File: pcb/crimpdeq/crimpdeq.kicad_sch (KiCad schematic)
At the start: 55 parts, among them J10 A-_Cable_Pad, J11 E+_Cable_Pad, J12 E-_Cable_Pad, J2 USB4105-GF-A, J5 B-_Cable_Pad, J6 SW+_Cable_Pad, J7 B+_Cable_Pad, J8 SW-_Cable_Pad, J9 A+_Cable_Pad, Q2 DMG3415U, U1 ESP32-C3-MINI-1, U2 MCP73831T-2ACI/OT, U3 ADS1220, U5 MAX17048G+T10, U6 SY8088

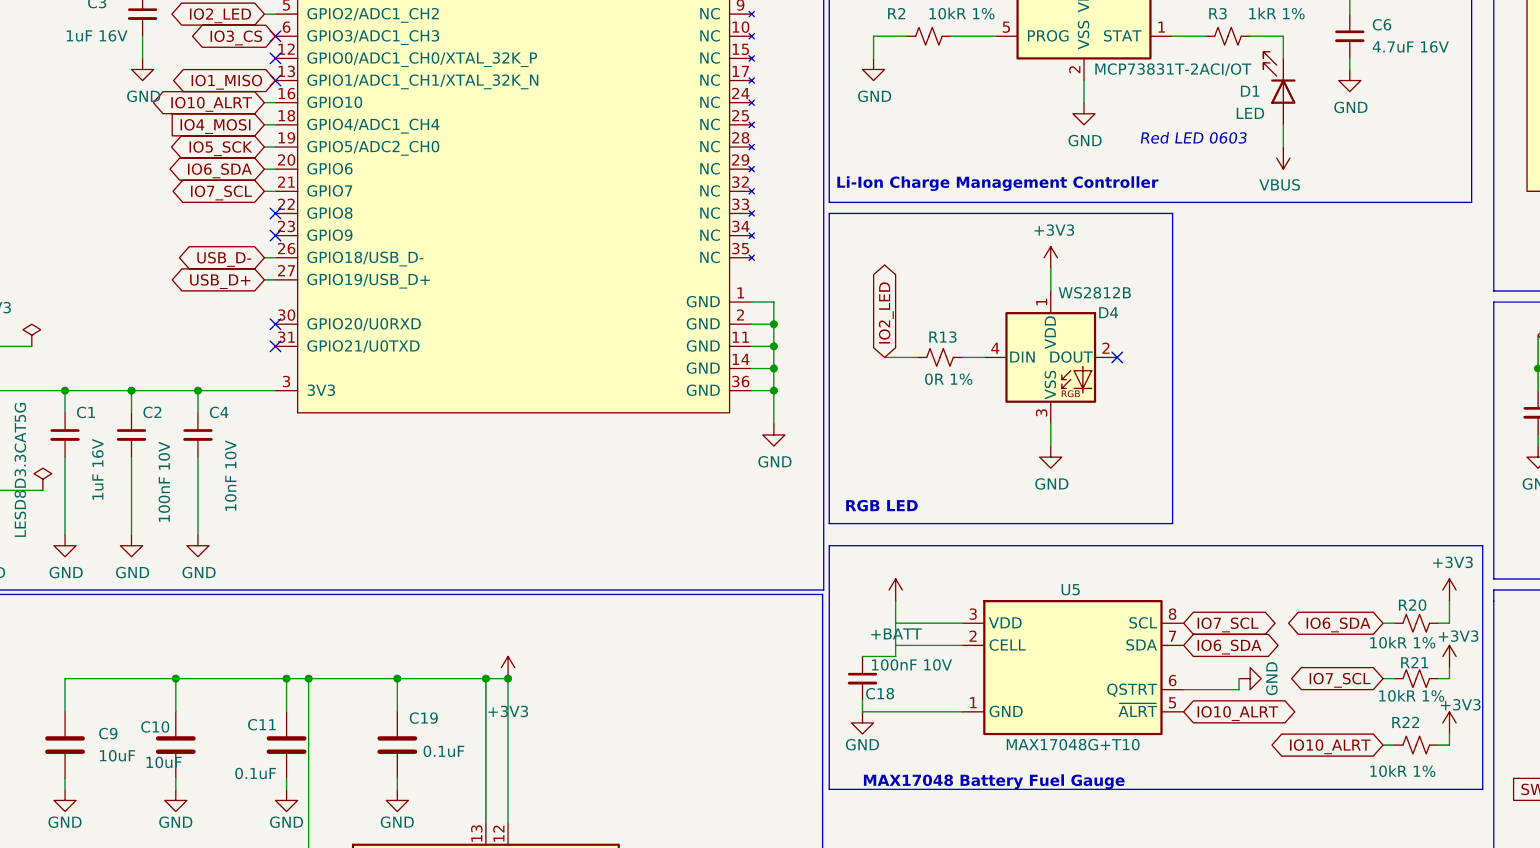
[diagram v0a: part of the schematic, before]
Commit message: fix: align MAX17048 I2C names with TDFN pads
Keep existing copper and GPIO numbers; rename the reversed SDA/SCL
labels and restore missing schematic paths so the board matches the
datasheet pin map.

Co-authored-by: Cursor <cursoragent@cursor.com>
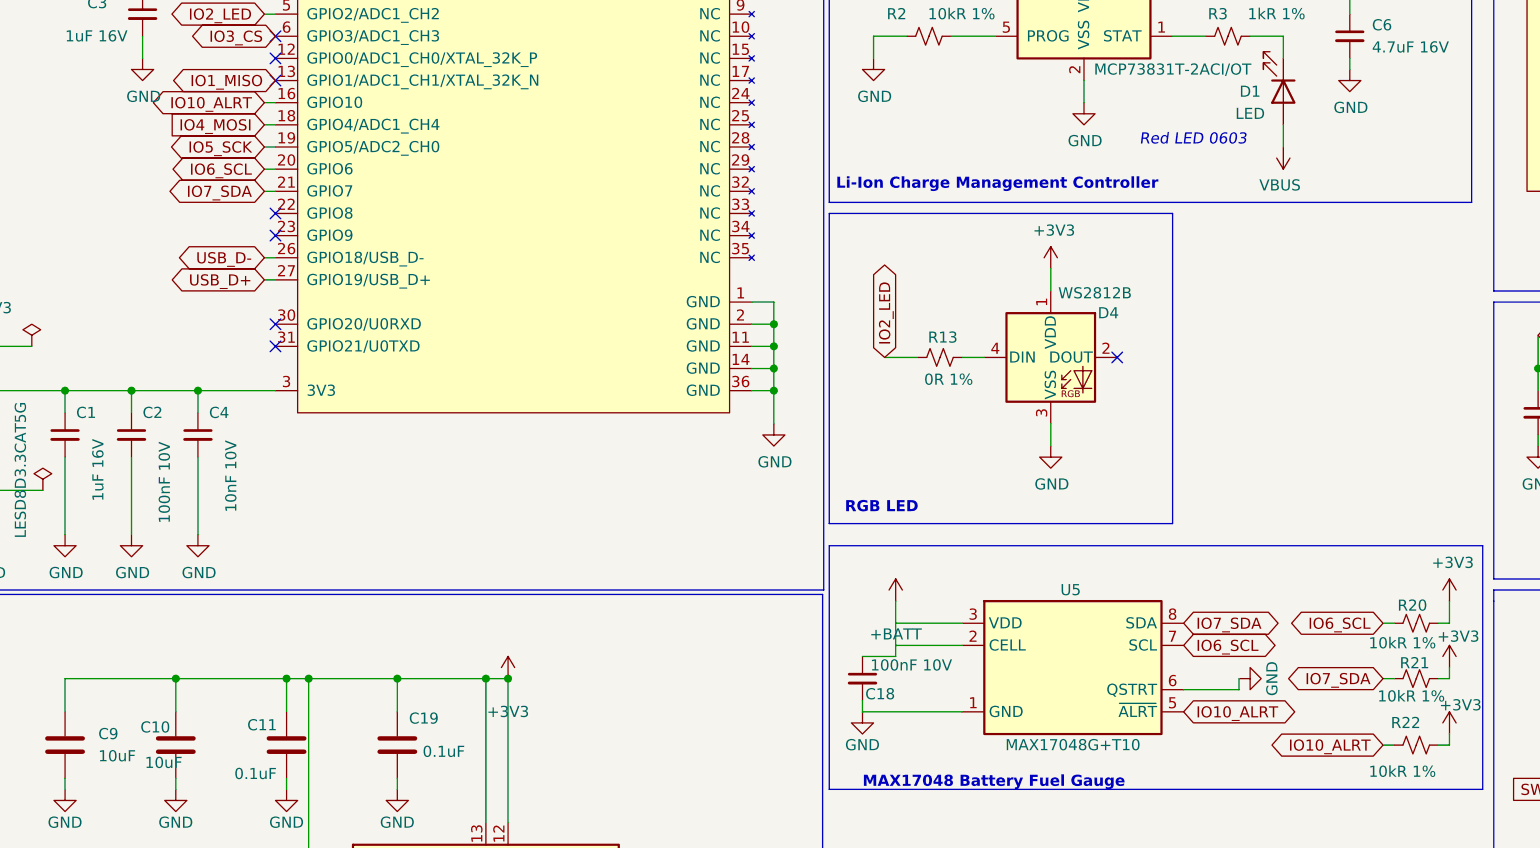
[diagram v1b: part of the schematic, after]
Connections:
- net IO6_SDA renamed IO6_SCL
- net IO7_SCL renamed IO7_SDA
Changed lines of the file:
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@@
 		)
 	)
-	(global_label "IO7_SCL"
+	(global_label "IO7_SDA"
 		(shape bidirectional)
 		(at 57.15 57.15 180)
@@
 		)
 	)
-	(global_label "IO6_SDA"
+	(global_label "IO6_SCL"
 		(shape bidirectional)
 		(at 185.42 106.68 180)
@@
 		)
 	)
-	(global_label "IO6_SDA"
+	(global_label "IO6_SCL"
 		(shape bidirectional)
 		(at 57.15 54.61 180)
@@
 		)
 	)
-	(global_label "IO7_SCL"
+	(global_label "IO7_SDA"
 		(shape bidirectional)
 		(at 162.56 106.68 0)
@@
 		)
 	)
-	(global_label "IO6_SDA"
+	(global_label "IO6_SCL"
 		(shape bidirectional)
 		(at 162.56 109.22 0)
@@
 		)
 	)
-	(global_label "IO7_SCL"
+	(global_label "IO7_SDA"
 		(shape bidirectional)
 		(at 185.42 113.03 180)
